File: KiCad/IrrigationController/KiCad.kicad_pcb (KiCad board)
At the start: 2 copper layers, 121.5 x 115 mm, 113 parts, among them IC1 MCP23017-E_SO, IC2 MCP23017-E_SO, IC3 DS89C21TMX_NOPB, J1 Screw_Terminal_01x03, J10 Screw_Terminal_01x05, J11 Screw_Terminal_01x02, J12 Screw_Terminal_01x02, J13 Screw_Terminal_01x04, J14 Screw_Terminal_01x02, J15 Screw_Terminal_01x02, J16 Screw_Terminal_01x02, J17 Screw_Terminal_01x02, J18 Screw_Terminal_01x02, J19 Screw_Terminal_01x02, J2 Screw_Terminal_01x03, J21 Screw_Terminal_01x06, J3 Screw_Terminal_01x03, J5 Screw_Terminal_01x03, J6 Screw_Terminal_01x02, J7 Screw_Terminal_01x02, J8 Screw_Terminal_01x02, J9 Screw_Terminal_01x02, K1 2071556-9, K2 2071556-9, Q1 MMBT3906, Q11 MMBT3904, Q12 MMBT3904, Q2 MMBT3906, Q3 MMBT3906, Q6 MMBT3904, Q7 MMBT3904, Q8 MMBT3904, SW1 SW_Push, U1 L298P, U2 ARDUINO_MKR_WAN_1310, U3 L298P, U4 L298P, U5 L298P, U7 L7805

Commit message: qwer
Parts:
- moved C13 3.79 mm to (168.2, 36.8), turned to 90 degrees
- moved U7 1.38 mm to (179.8, 30.5)
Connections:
- U1 pad 21: (no net) -> Earth
- U3 pad 21: (no net) -> Earth
- U4 pad 21: (no net) -> Earth
- U5 pad 21: (no net) -> Earth
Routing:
- net Earth: track 329.3 -> 545.0 mm, vias 23 -> 85
- net +12V: track 526.8 -> 522.6 mm
- net /Vin: track 70.9 -> 67.8 mm

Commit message: pcb donde
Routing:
- net Earth: track 545.0 -> 405.8 mm, vias 85 -> 42

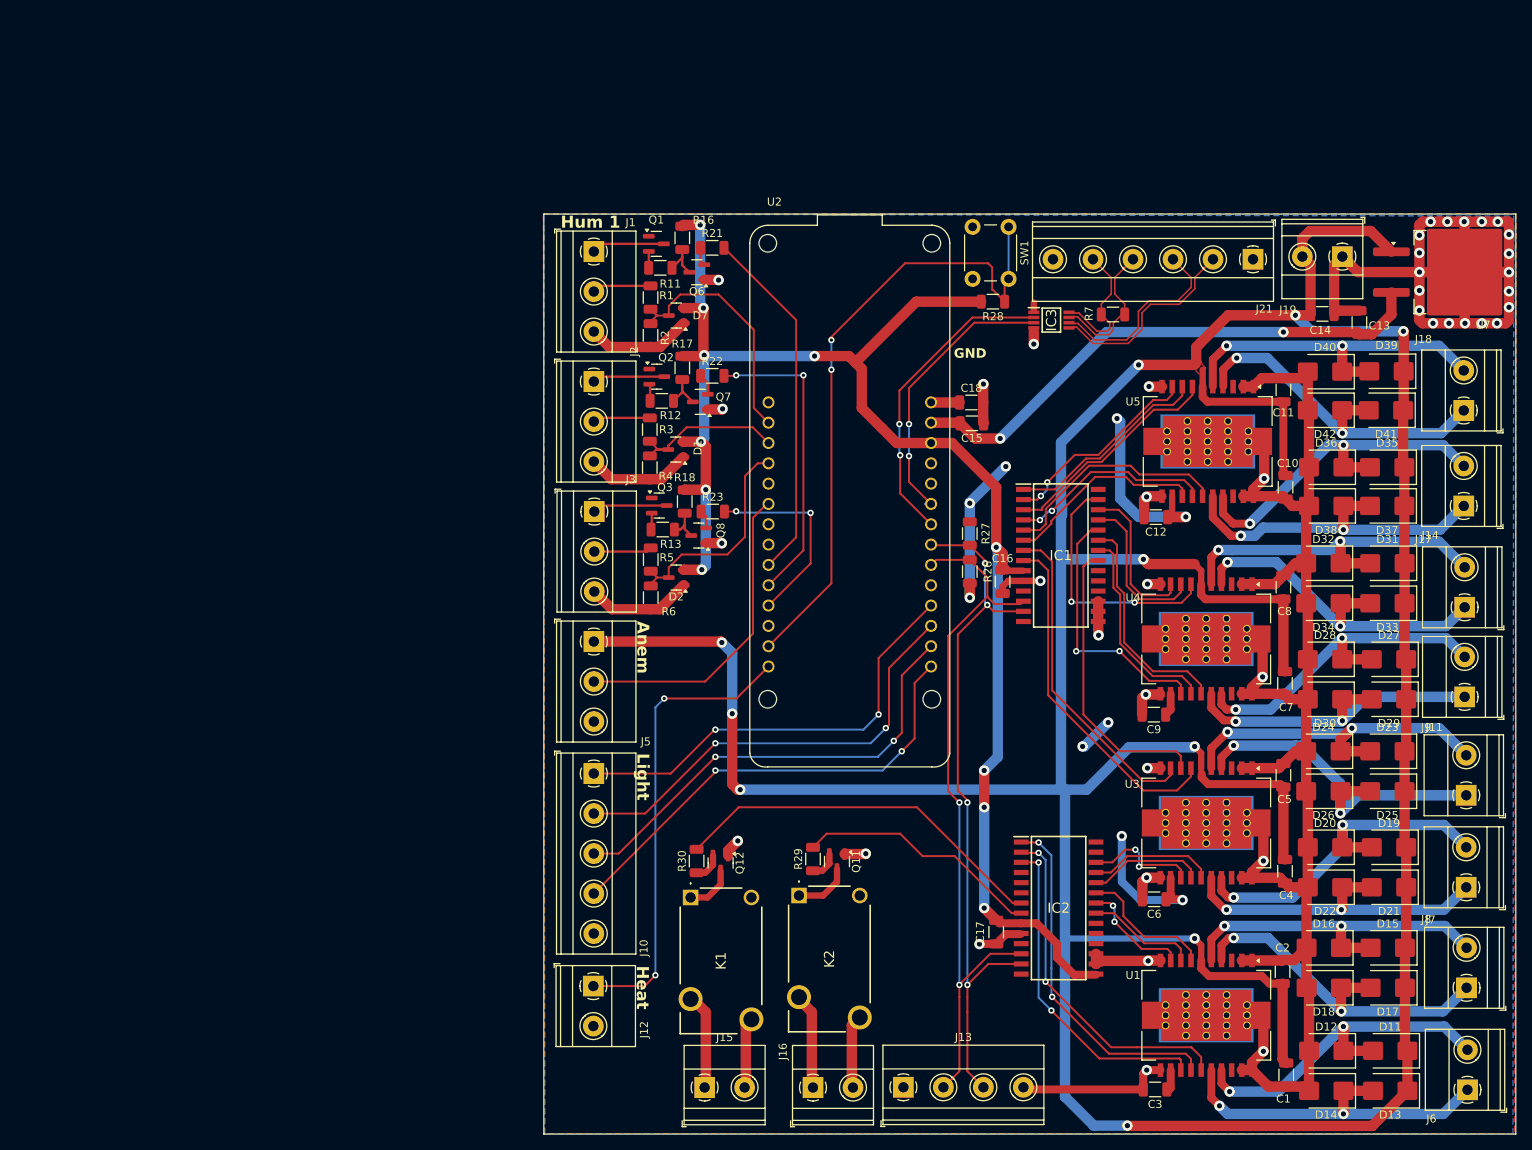
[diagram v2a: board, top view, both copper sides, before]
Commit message: Arregladas las conexiones al plano de masa
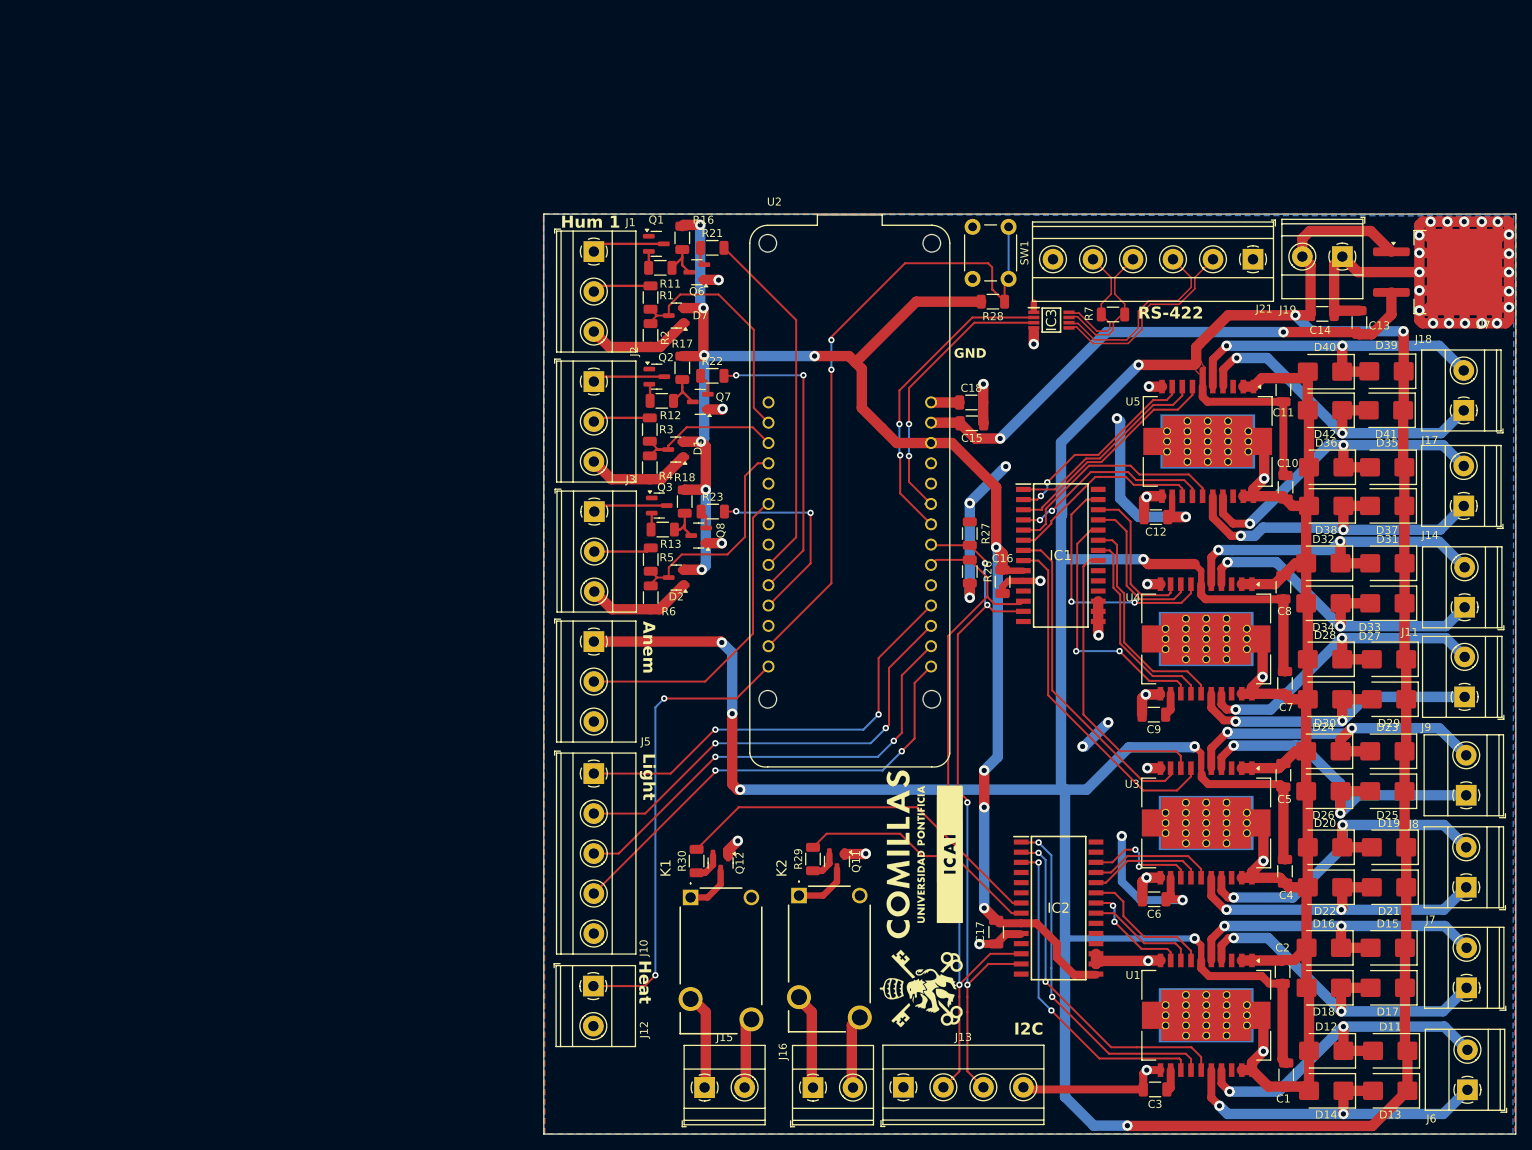
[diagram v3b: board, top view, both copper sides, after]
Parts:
- added G***: LOGO, MisHuellas:Logo-ICAI, F.Cu at (113.5, 109.0)
- added REF**: KiCad-Logo2_12mm_SilkScreen, Symbol:KiCad-Logo2_12mm_SilkScreen, B.Cu at (128.0, 82.5)
- C16, C17, C18: value 100n -> 0.1u
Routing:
- net Earth: track 405.8 -> 523.3 mm
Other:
- board text added: "I2C"
- board text added: "RS-422"

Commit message: fixed last minute error on PCB + continued Arduino development
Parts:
- removed J21: Screw_Terminal_01x06, TerminalBlock_Phoenix:TerminalBlock_Phoenix_MKDS-1,5-6_1x06_P5.00mm_Horizontal
- added J4: 691382030006, SimbolosSnapEDA:691382030006, F.Cu at (141.1, 28.0)
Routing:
- net /D0-: track 24.6 -> 21.3 mm
- net /D0+: track 25.3 -> 22.0 mm
- net /RI-: track 16.8 -> 17.6 mm
- net /RI+: track 17.9 -> 18.8 mm

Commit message: q
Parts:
- removed J4: 691382030006, SimbolosSnapEDA:691382030006
- added J21: Screw_Terminal_01x06, TerminalBlock_Phoenix:TerminalBlock_Phoenix_MKDS-1,5-6_1x06_P5.00mm_Horizontal, F.Cu at (154.9, 28.9)
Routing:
- net /D0-: track 21.3 -> 24.6 mm
- net /D0+: track 22.0 -> 25.3 mm
- net /RI-: track 17.6 -> 16.8 mm
- net /RI+: track 18.8 -> 17.9 mm

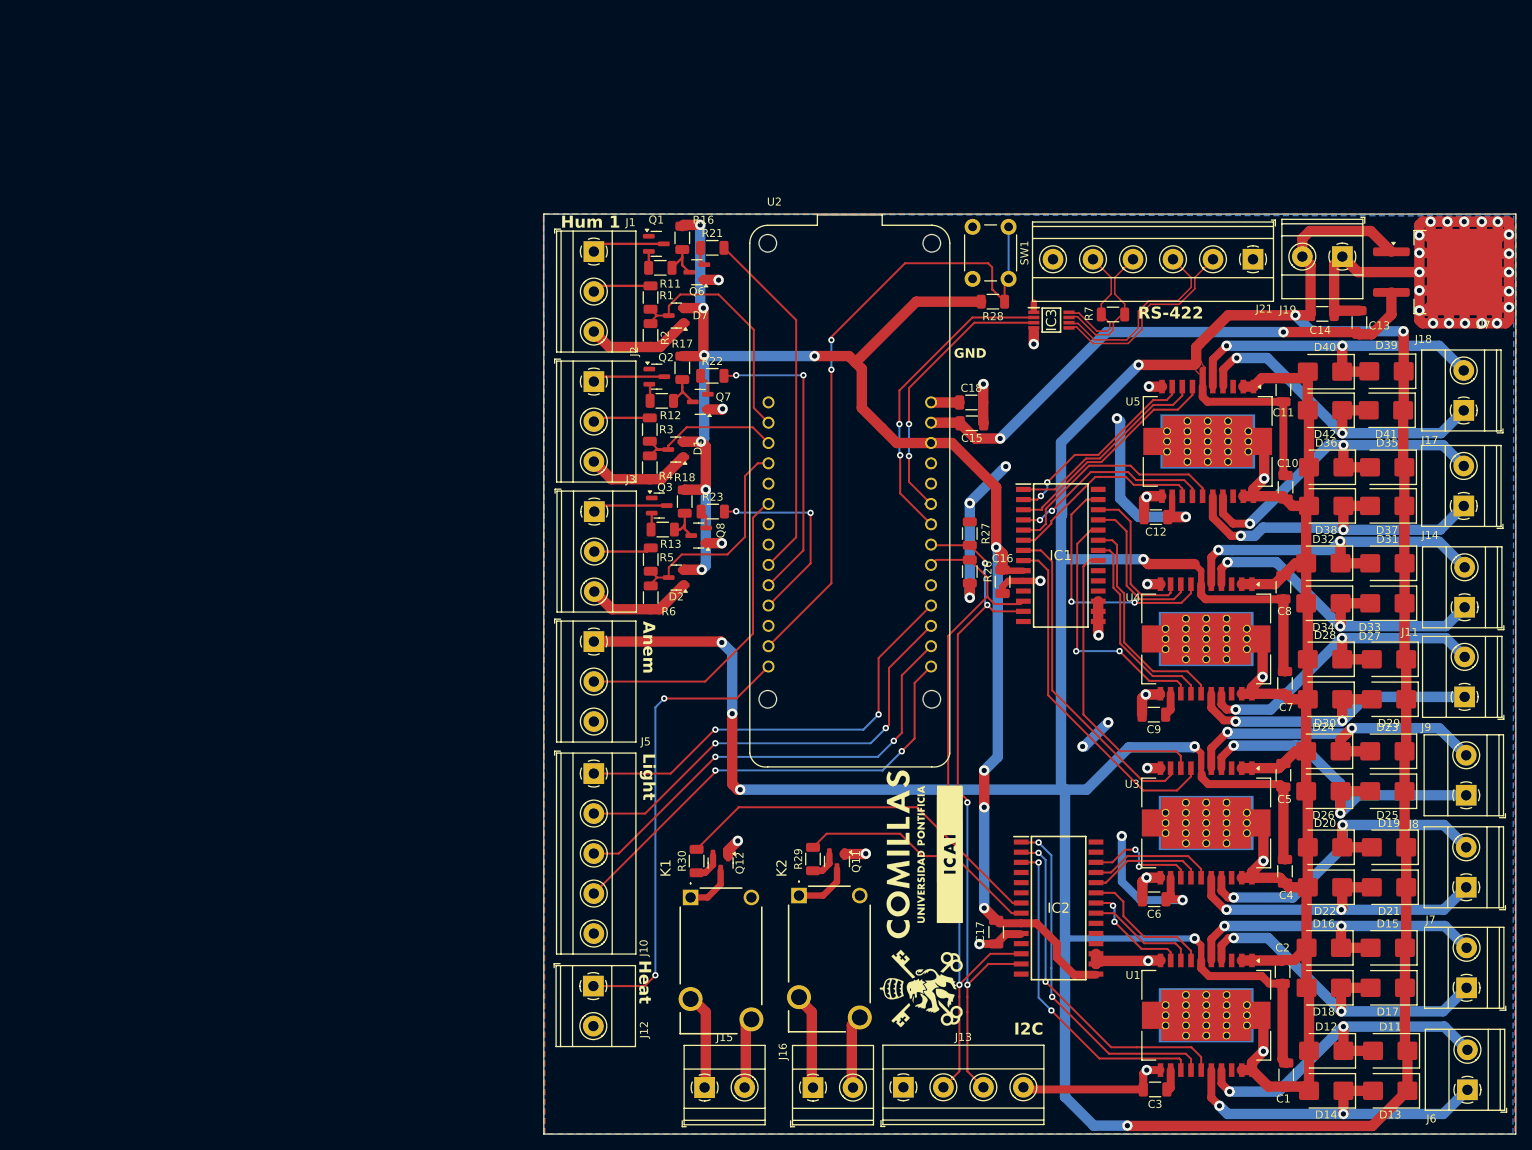
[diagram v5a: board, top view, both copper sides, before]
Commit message: fixed error on I2C lines
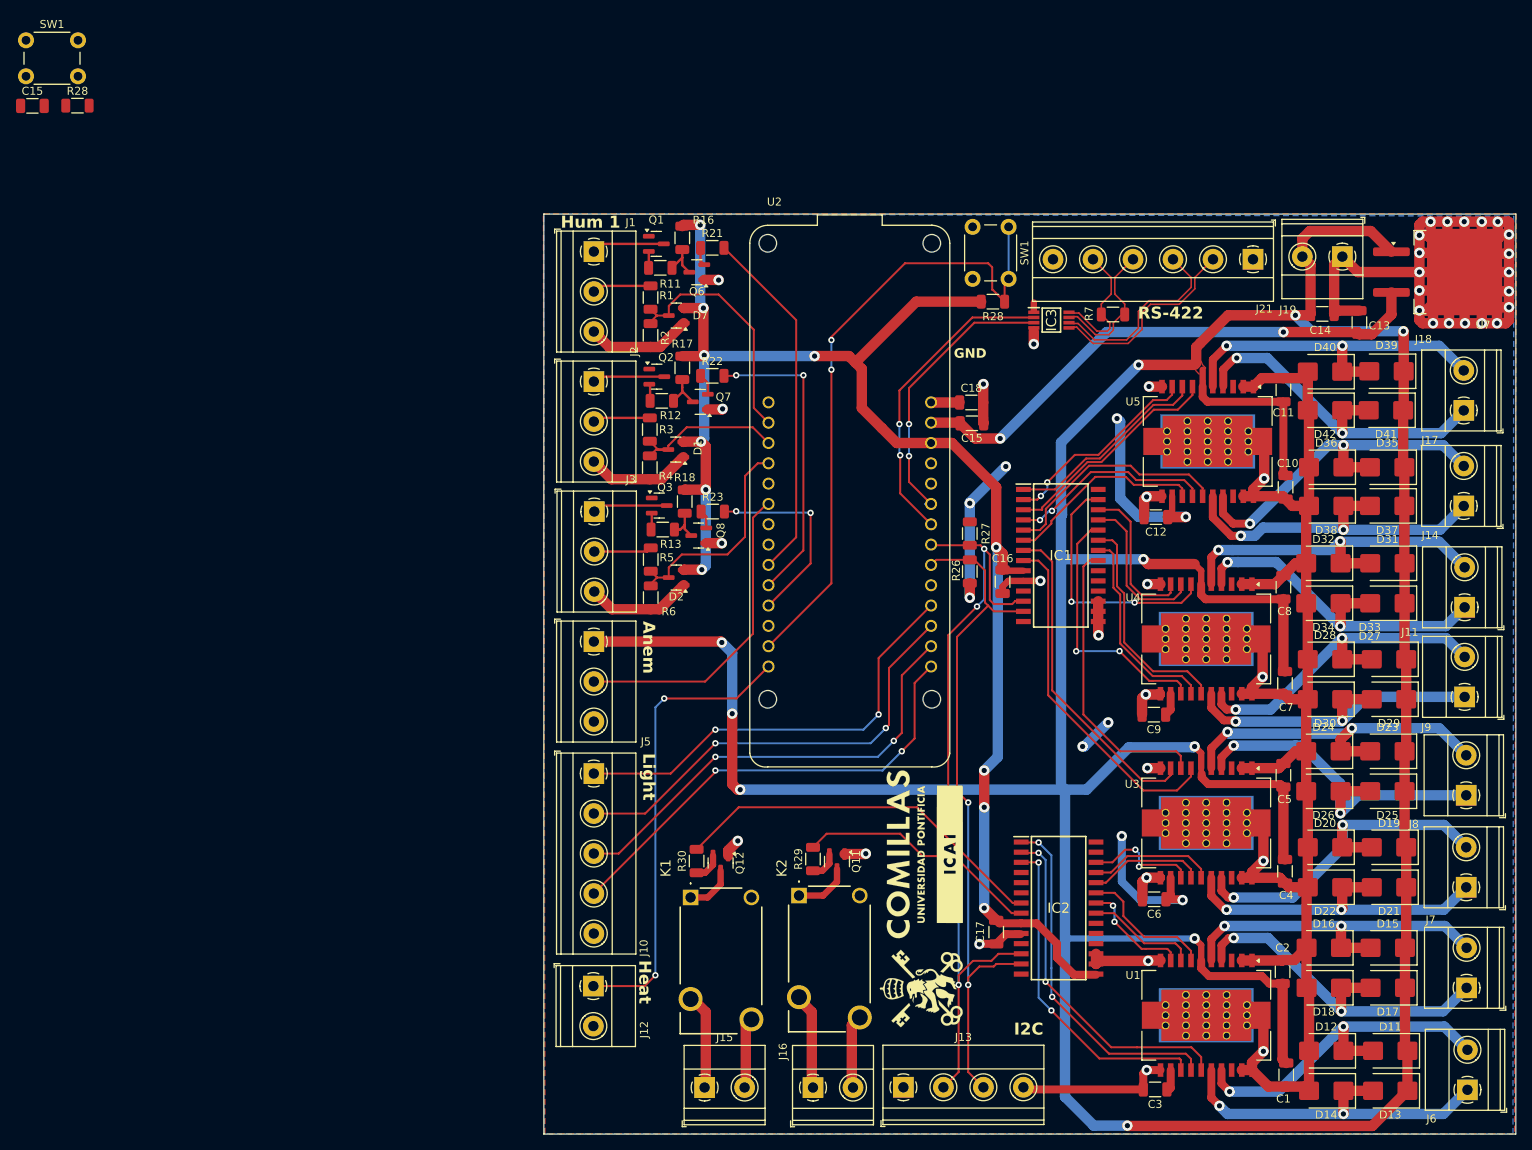
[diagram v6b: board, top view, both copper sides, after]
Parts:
- added C15: 0.1u, Capacitor_SMD:C_1206_3216Metric, F.Cu at (2.33, 9.72)
- added R28: 10k, Resistor_SMD:R_1206_3216Metric, F.Cu at (7.96, 9.70)
- added SW1: SW_Push, Button_Switch_THT:SW_PUSH_6mm_H4.3mm, F.Cu at (1.52, 1.52)
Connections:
- IC1 pad 12: /SDA -> /SCL
- IC1 pad 13: /SCL -> /SDA
- IC2 pad 12: /SDA -> /SCL
- IC2 pad 13: /SCL -> /SDA
- J13 pad 2: /SDA -> /SCL
- J13 pad 3: /SCL -> /SDA
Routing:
- net /SCL: track 89.0 -> 98.7 mm
- net /SDA: track 89.8 -> 88.2 mm
